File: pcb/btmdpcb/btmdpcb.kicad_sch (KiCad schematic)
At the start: 34 parts, among them Q4 AO3401A, Q5 AO3401A, Q6 BSD235C, Q8 BSD235C

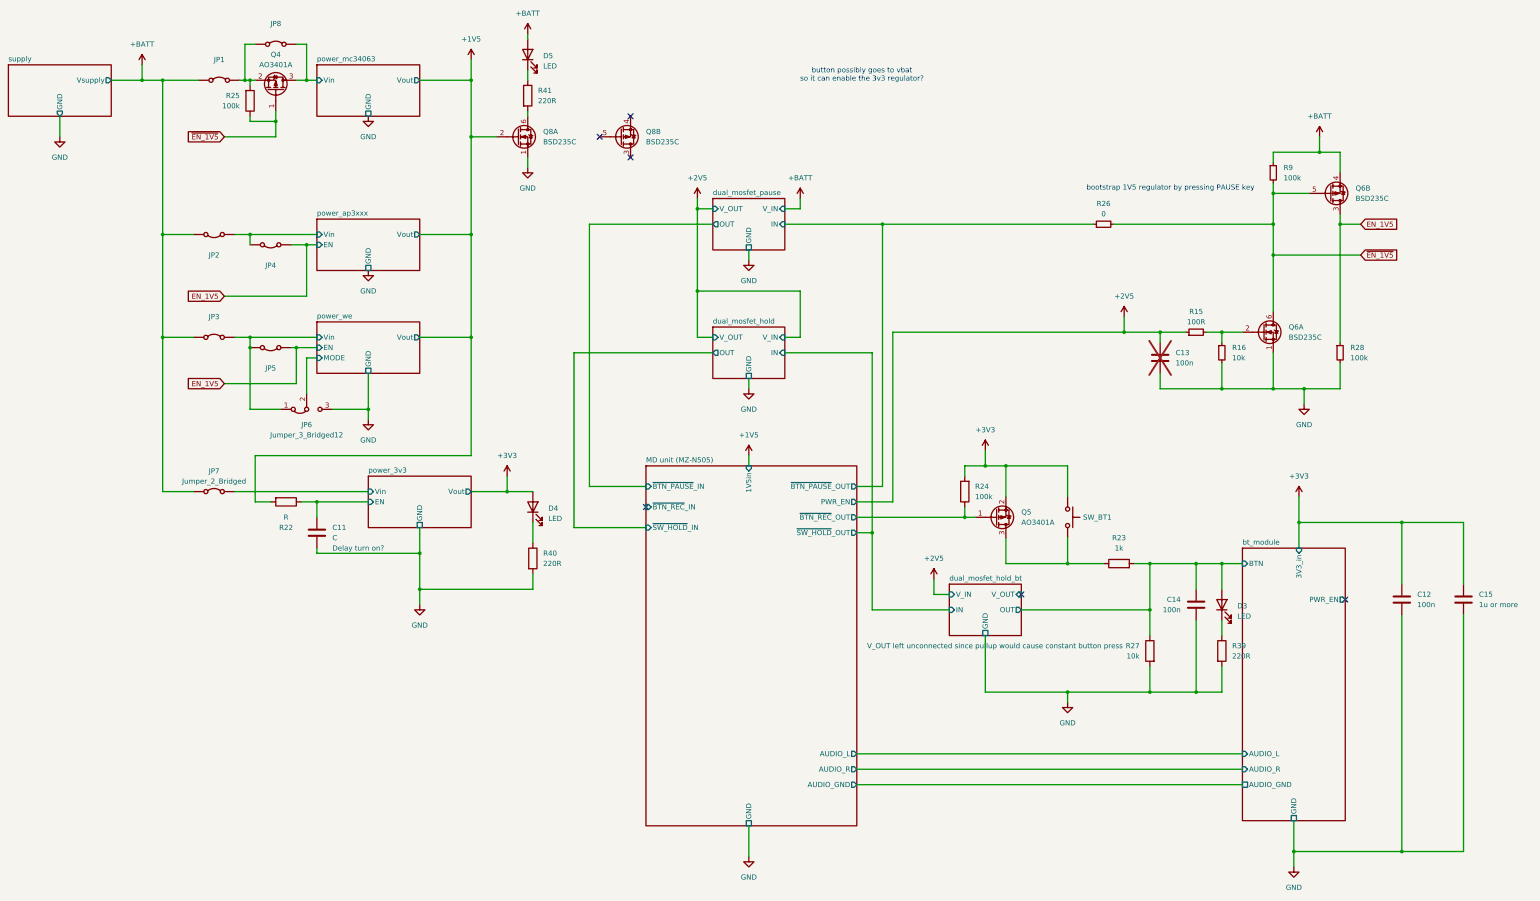
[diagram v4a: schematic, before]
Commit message: Clean up schematic, implement all logic functionality
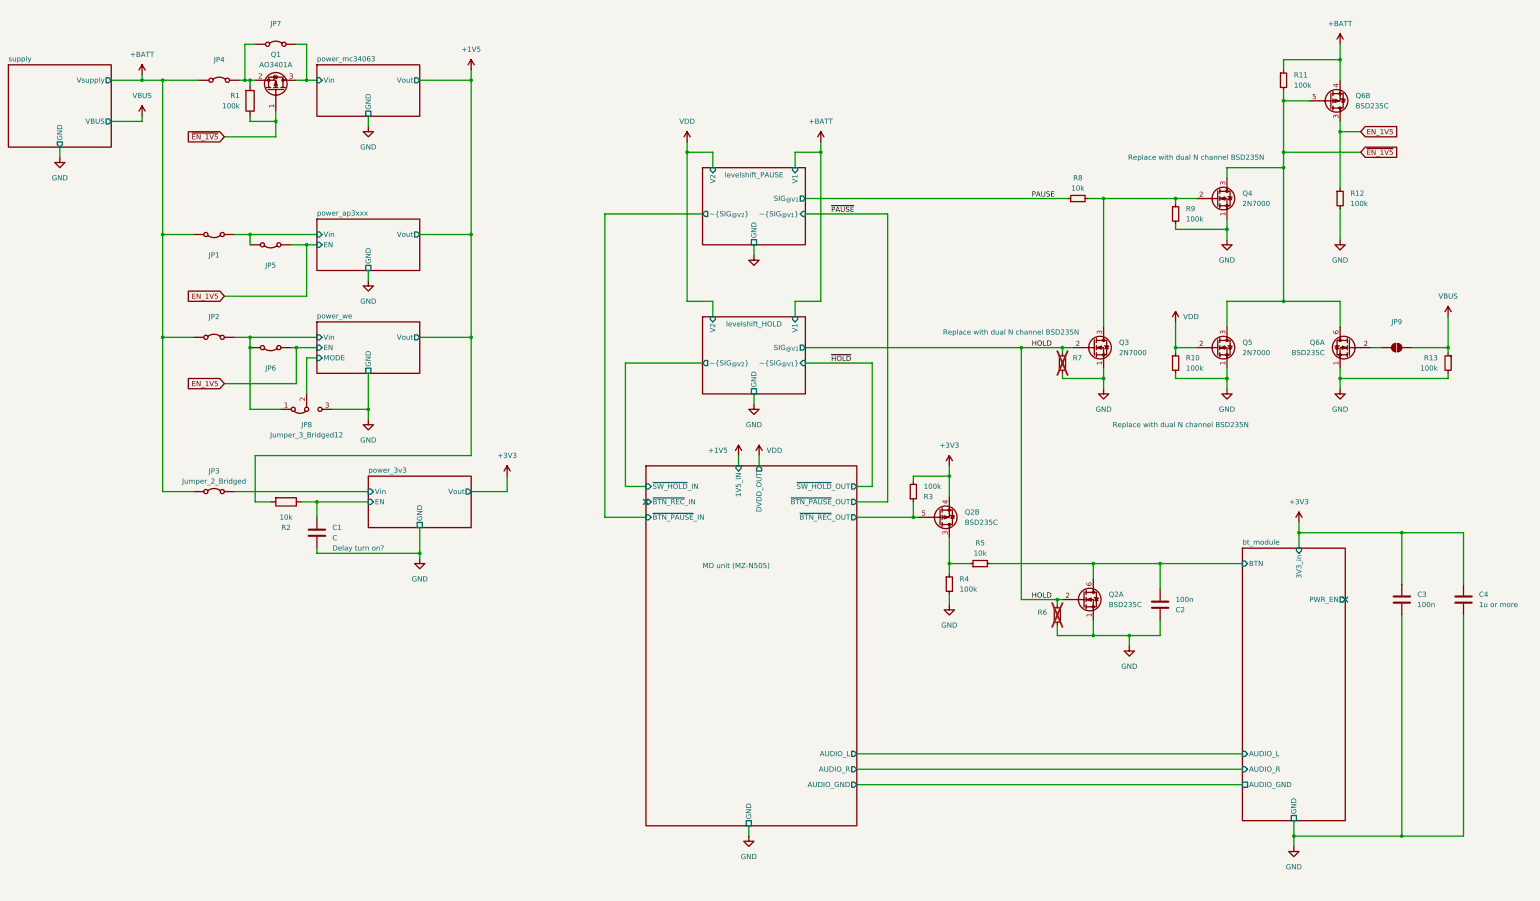
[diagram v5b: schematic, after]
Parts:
- removed C13: 100n, symbol Device:C
- removed D3, D4, D5: LED, symbol Device:LED
- removed Q5: AO3401A, Package_TO_SOT_SMD:SOT-23, symbol Transistor_FET:AO3401A
- removed Q8: BSD235C, Package_TO_SOT_SMD:SOT-363_SC-70-6, symbol Transistor_FET:BSD235C
- removed R15: 100R, symbol Device:R_Small
- removed R22: R, symbol Device:R
- removed R23: 1k, symbol Device:R
- removed R24: 100k, symbol Device:R
- removed R26: 0, symbol Device:R_Small
- removed R27: 10k, symbol Device:R
- removed R39, R40, R41: 220R, symbol Device:R
- removed SW_BT1: SW_Push, symbol Switch:SW_Push
- added JP9: SolderJumper_2_Open, Jumper:SolderJumper-2_P1.3mm_Open_RoundedPad1.0x1.5mm, symbol Jumper:SolderJumper_2_Open
- added Q2: BSD235C, Package_TO_SOT_SMD:SOT-363_SC-70-6, symbol Transistor_FET:BSD235C
- added Q3, Q4, Q5: 2N7000, Package_TO_SOT_THT:TO-92_Inline, symbol Transistor_FET:2N7000
- added R13, R3, R4, R9: 100k, symbol Device:R_Small
- added R2: 10k, symbol Device:R
- added R5, R8: 10k, symbol Device:R_Small
- added R6, R7: ~, symbol Device:R_Small
- R10: renamed from R16; value 10k -> 100k
- renumbered C11 to C1, C14 to C2, C12 to C3, C15 to C4, JP2 to JP1, JP3 to JP2, JP7 to JP3, JP1 to JP4, JP4 to JP5, JP5 to JP6, JP8 to JP7, JP6 to JP8, Q4 to Q1, R25 to R1, R9 to R11, R28 to R12
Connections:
- net +1V5: now also R2.2
- net +3V3: now also Q2.4 (SP), R3.2
- net GND: now also C2.1, Q2.1 (SN), Q3.1 (S), Q4.1 (S), Q5.1 (S), R13.2, R4.2, R6.2, R7.2, R9.2; no longer C2.2
- net MD unit (MZ-N505)/~{BTN_REC}_OUT: now also Q2.5 (GP), R3.1
- net bt_module/BTN: now also C2.2, Q2.6 (DN), R5.2; no longer C2.1
- net power_3v3/EN: now also R2.1
- net ~{EN_1V5}: now also Q4.3 (D), Q5.3 (D)
- net at Q6.2 (GN): now also JP9.1 (A); no longer R10.1
- new net: Q2.3 (DP), R4.1, R5.1
- new net: Q3.3 (D), Q4.2 (G), R8.2, R9.1
- new net HOLD: Q2.2 (GN), Q3.2 (G), R6.1, R7.1
- new net PAUSE: R8.1
- new net VBUS: JP9.2 (B), R13.1
- new net VDD: Q5.2 (G), R10.1
- no-connect marks 6 -> 2
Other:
- sheet dual_mosfet_hold renamed levelshift_HOLD
- sheet dual_mosfet_pause renamed levelshift_PAUSE
- removed sheet dual_mosfet_hold_bt
- sheet MD unit (MZ-N505) ports: added 1V5_IN, DVDD_OUT; removed 1V5in, PWR_EN
- sheet levelshift_HOLD ports: added SIG_{@V1}, V1, V2, ~{SIG_{@V1}}, ~{SIG_{@V2}}; removed IN, OUT, V_IN, V_OUT
- sheet levelshift_PAUSE ports: added SIG_{@V1}, V1, V2, ~{SIG_{@V1}}, ~{SIG_{@V2}}; removed IN, OUT, V_IN, V_OUT
- sheet supply ports: added VBUS; removed none
- note removed: "bootstrap 1V5 regulator by pressing PAUSE key"
- note removed: "button possibly goes to vbat so it can enable the 3v3 regulator?"
- moved on the sheet: C2, Q6A, Q6B, R10, R11, R12

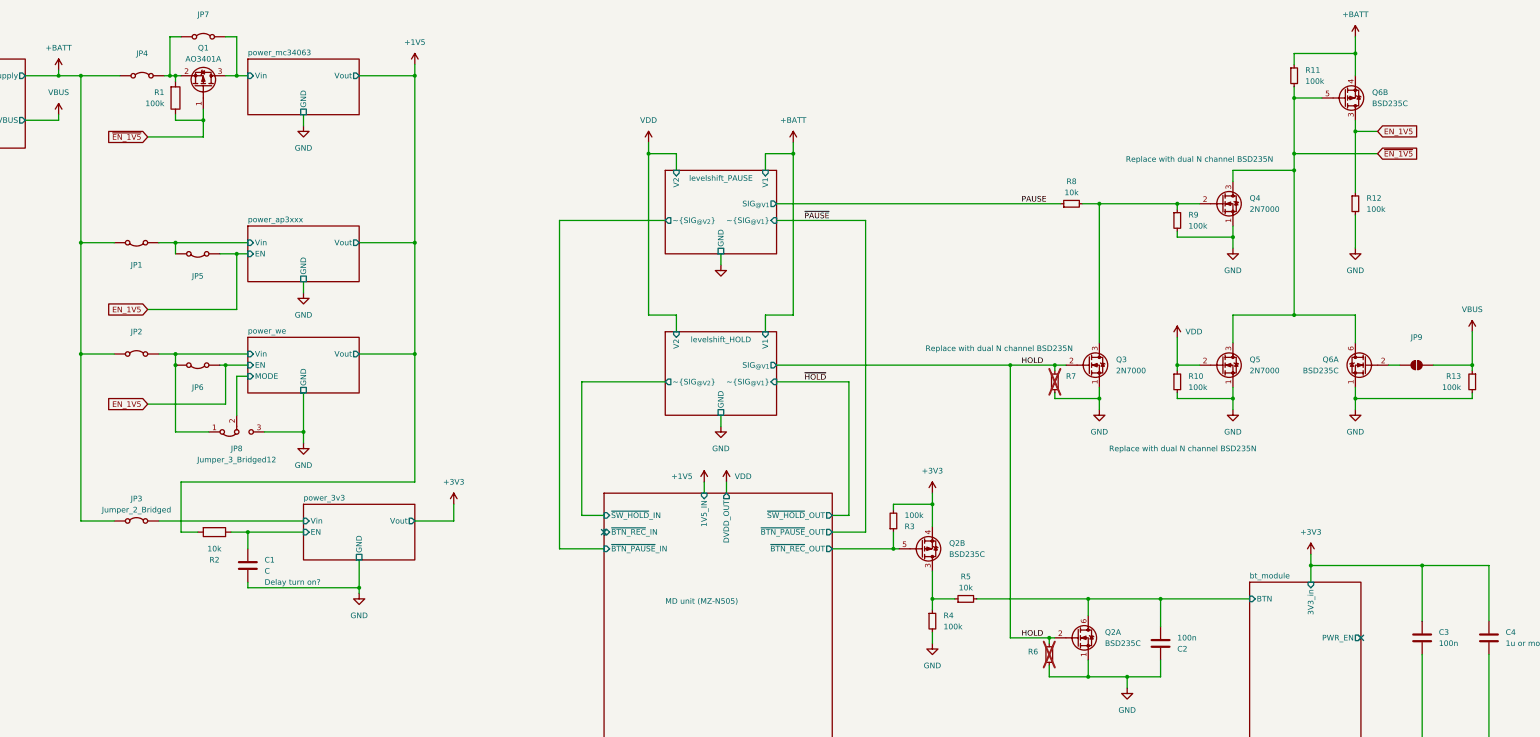
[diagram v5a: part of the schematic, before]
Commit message: Remove redundant regulators, simplify schematic
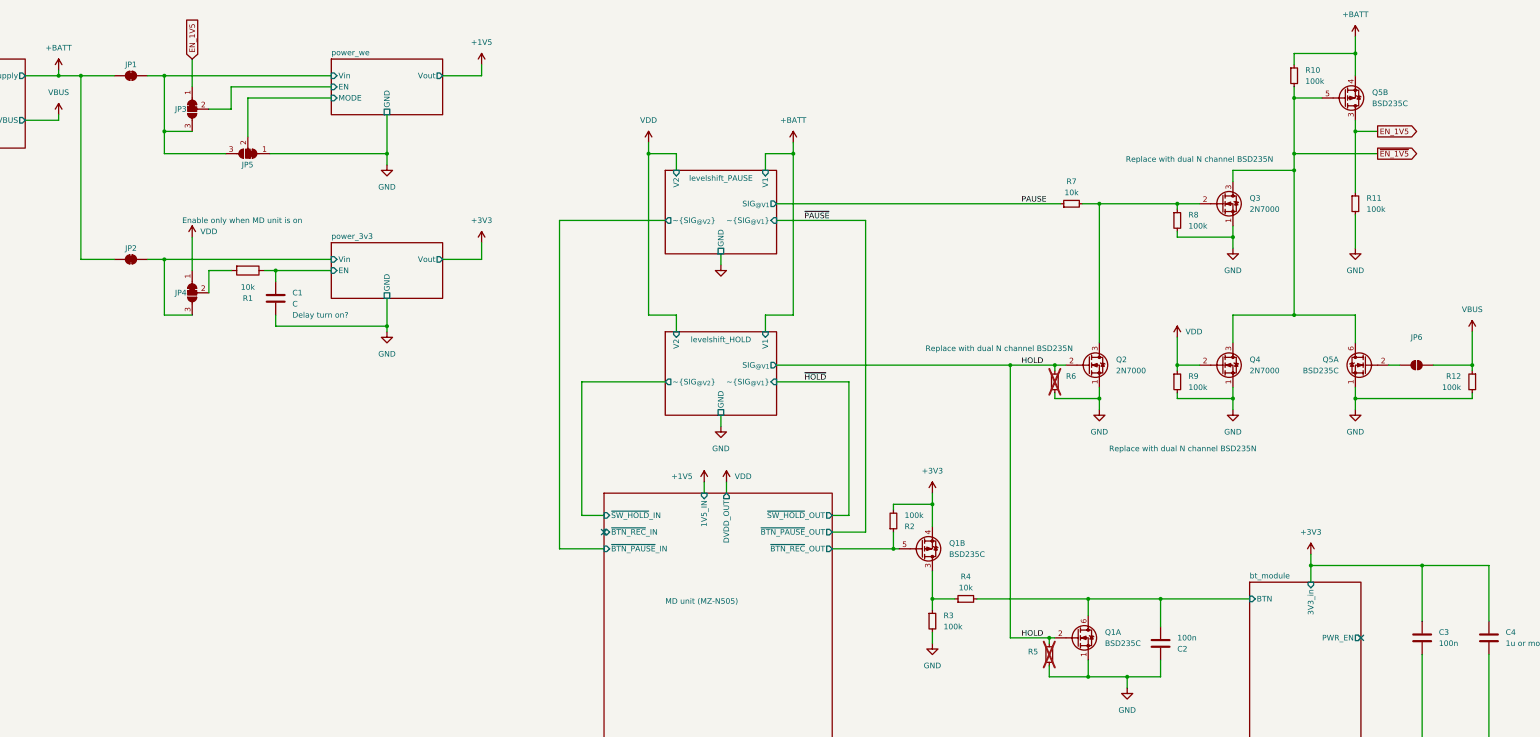
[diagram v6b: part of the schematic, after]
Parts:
- removed JP1, JP2, JP3, JP4, JP5, JP6, JP7: Jumper_2_Bridged, symbol Jumper:Jumper_2_Bridged
- removed JP8: Jumper_3_Bridged12, symbol Jumper:Jumper_3_Bridged12
- removed Q1: AO3401A, Package_TO_SOT_SMD:SOT-23, symbol Transistor_FET:AO3401A
- removed R1: 100k, symbol Device:R
- added JP1, JP2: SolderJumper_2_Bridged, Jumper:SolderJumper-2_P1.3mm_Bridged_RoundedPad1.0x1.5mm, symbol Jumper:SolderJumper_2_Bridged
- added JP3, JP4, JP5: SolderJumper_3_Bridged12, symbol Jumper:SolderJumper_3_Bridged12
- renumbered JP9 to JP6, Q2 to Q1, Q3 to Q2, Q4 to Q3, Q5 to Q4, Q6 to Q5, R2 to R1, R11 to R10, R12 to R11, R13 to R12, R3 to R2, R4 to R3, R5 to R4, R6 to R5, R7 to R6, R8 to R7, R9 to R8, R10 to R9
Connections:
- net +1V5: no longer R1.2
- net +BATT: now also JP1.1 (A), JP2.1 (A)
- net EN_1V5: now also JP3.1 (A)
- net GND: now also JP5.1 (A)
- net VDD: now also JP4.1 (A)
- net power_3v3/Vin: now also JP2.2 (B), JP4.3 (B)
- net power_we/MODE: now also JP5.2 (C)
- net power_we/Vin: now also JP1.2 (B), JP3.3 (B), JP5.3 (B)
- new net: JP4.2 (C), R1.2
- new net power_we/EN: JP3.2 (C)
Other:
- removed sheet power_ap3xxx
- removed sheet power_mc34063
- moved on the sheet: C1, R1

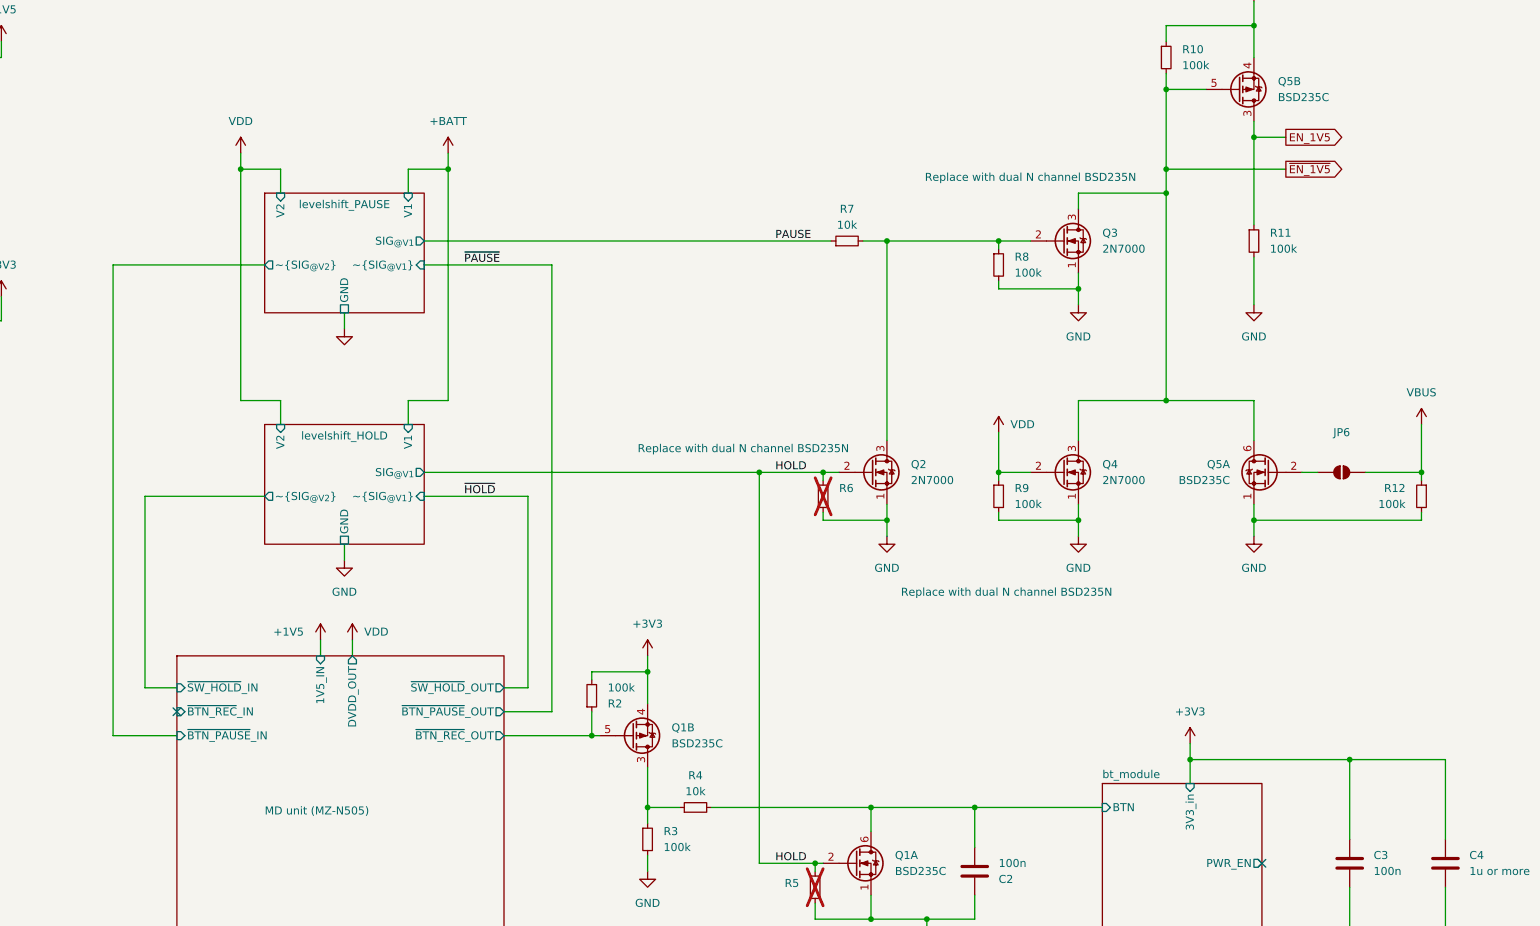
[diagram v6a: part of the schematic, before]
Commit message: Use REC instead of PAUSE for power kickstart
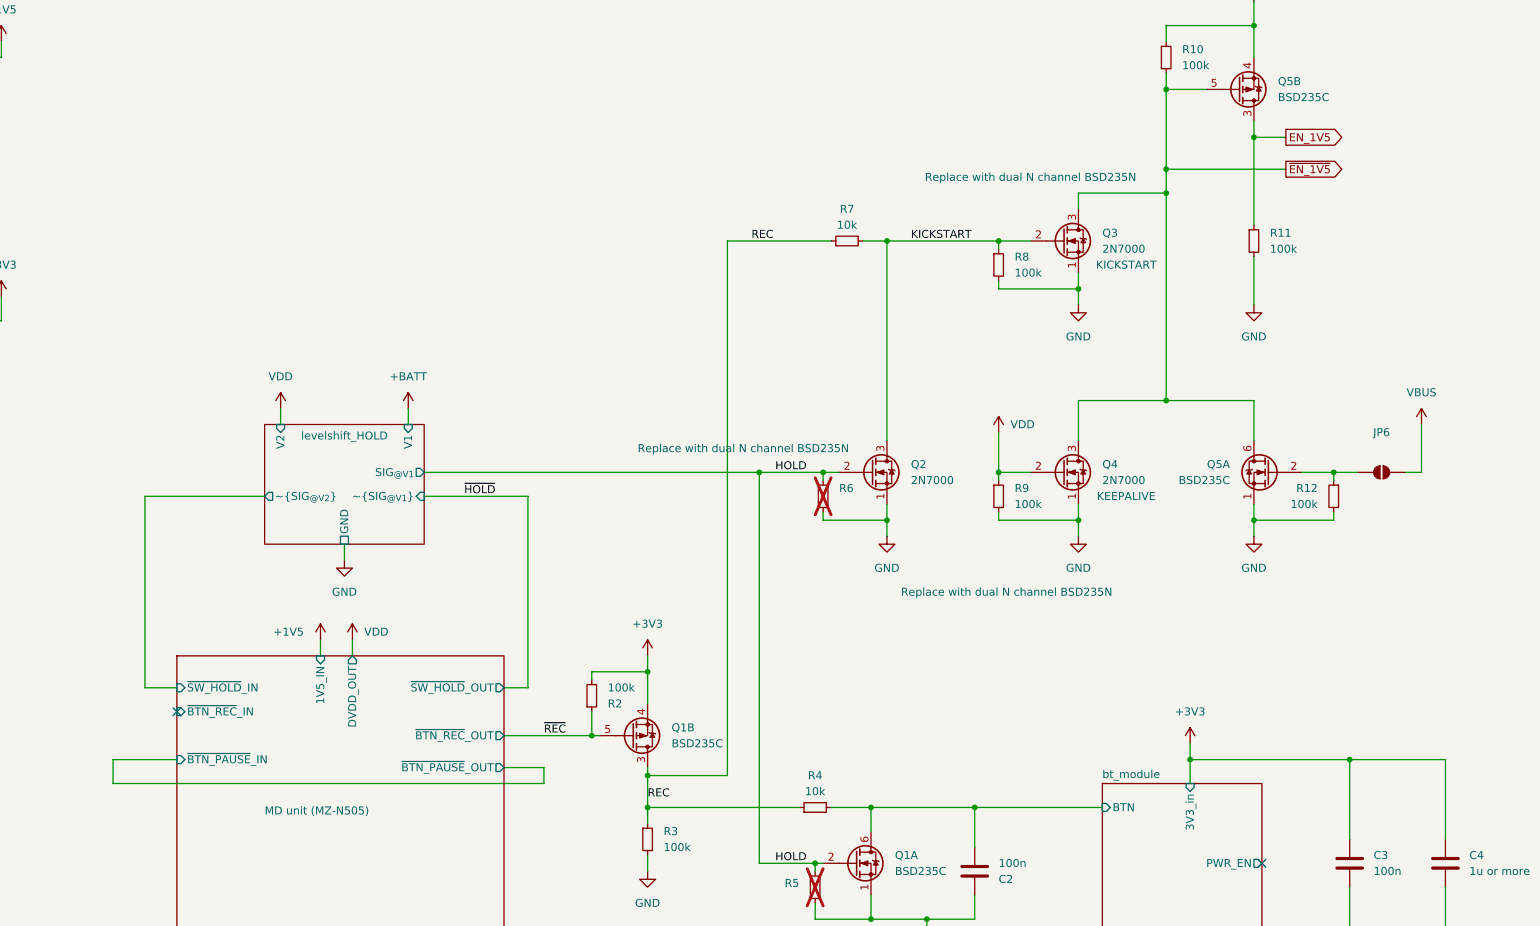
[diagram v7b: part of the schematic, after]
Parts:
- Q3: Function (none) -> KICKSTART
- Q4: Function (none) -> KEEPALIVE
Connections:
- net PAUSE is gone; now on net REC: R7.1
- net VBUS: no longer R12.1
- net REC: now reaches Q1.3 (DP), R3.1, R4.1
- net at JP6.1 (A), Q5.2 (GN): now also R12.1
- net KICKSTART: now reaches Q2.3 (D), Q3.2 (G), R7.2, R8.1
- net MD unit (MZ-N505)/~{BTN_REC}_OUT renamed ~{REC}
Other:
- removed sheet levelshift_PAUSE
- moved on the sheet: JP6, R12, R4
